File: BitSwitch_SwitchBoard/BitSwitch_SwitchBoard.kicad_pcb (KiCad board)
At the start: 2 copper layers, 116.2 x 17.1 mm, 23 parts, among them J1 Conn_01x05_Pin, J2 Conn_01x05_Pin, SW1 SW_Push_Open, SW2 SW_Push_Open, SW3 SW_Push_Open, SW4 SW_Push_Open, SW5 SW_Push_Open, SW6 SW_Push_Open, SW7 SW_Push_Open, SW8 SW_Push_Open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

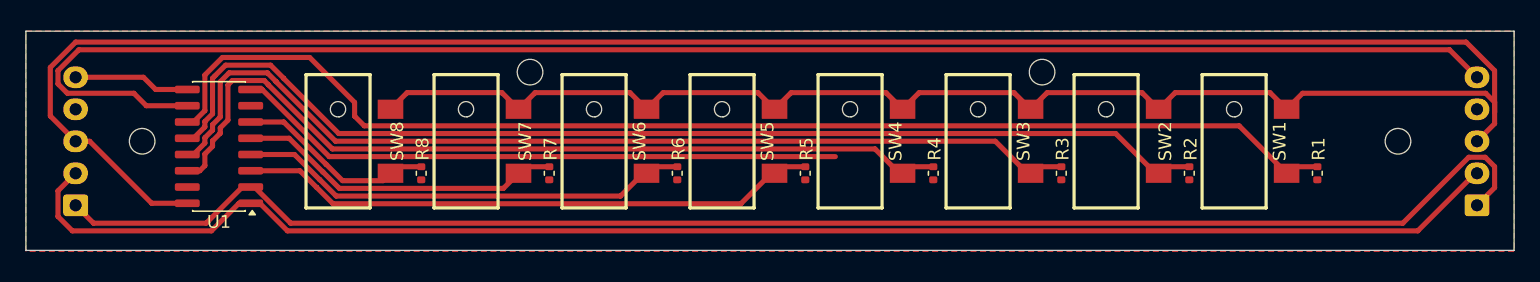
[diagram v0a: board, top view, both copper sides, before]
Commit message: Adjust board size
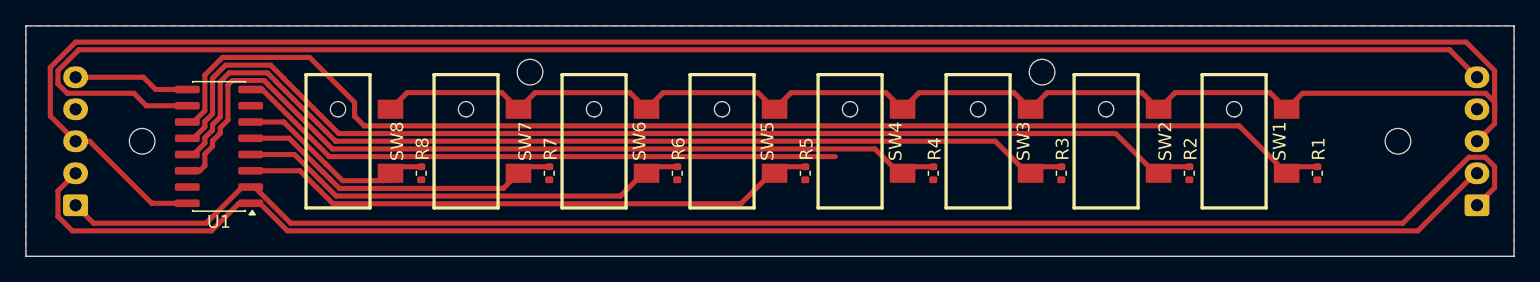
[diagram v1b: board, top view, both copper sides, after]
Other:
- board size 116.2 x 17.1 mm -> 116.2 x 18 mm
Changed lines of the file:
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@@
 		(filling no)
 		(zone_defaults)
+		(grid_origin 44.32 58.1)
 		(pcbplotparams
 			(layerselection 0x00000000_00000000_55555555_5755f5ff)
@@
 	)
 	(gr_rect
-		(start 44.32 58.51)
-		(end 160.57 75.635)
+		(start 44.32 58.1)
+		(end 160.57 76.1)
 		(stroke
 			(width 0.05)
@@
 		(polygon
 			(pts
-				(xy 160.57 75.71) (xy 44.32 75.71) (xy 44.32 58.51) (xy 160.57 58.51)
+				(xy 160.57 76.1) (xy 44.32 76.1) (xy 44.32 58.1) (xy 160.57 58.1)
 			)
 		)
